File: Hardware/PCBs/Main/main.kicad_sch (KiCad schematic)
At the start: 141 parts, among them J2 HARWIN M20-8890545R, J3 USB4110-GF-A, J4 F3311A7H121010E200, SW1 TL1014BF160QG, SW10 EVPBT1C4A000, SW11 EVPBT1C4A000, SW12 EVPBT1C4A000, SW13 EVPBT1C4A000, SW14 EVPBT1C4A000, SW15 EVPBT1C4A000, SW16 EVPBT1C4A000, SW17 EVPBT1C4A000, SW18 EVPBT1C4A000, SW19 EVPBT1C4A000, SW2 CUS-12TB, SW20 EVPBT1C4A000, SW21 EVPBT1C4A000, SW22 EVPBT1C4A000, SW23 EVPBT1C4A000, SW24 EVPBT1C4A000, SW25 EVPBT1C4A000, SW26 EVPBT1C4A000, SW27 EVPBT1C4A000, SW28 EVPBT1C4A000, SW29 EVPBT1C4A000, SW3 EVPBT1C4A000, SW30 EVPBT1C4A000, SW31 EVPBT1C4A000, SW32 EVPBT1C4A000, SW33 EVPBT1C4A000, SW34 EVPBT1C4A000, SW35 EVPBT1C4A000, SW36 EVPBT1C4A000, SW37 EVPBT1C4A000, SW38 EVPBT1C4A000, SW39 EVPBT1C4A000, SW4 EVPBT1C4A000, SW40 EVPBT1C4A000, SW41 EVPBT1C4A000, SW42 EVPBT1C4A000, SW43 EVPBT1C4A000, SW44 EVPBT1C4A000, SW45 EVPBT1C4A000, SW46 EVPBT1C4A000, SW47 EVPBT1C4A000, SW48 EVPBT1C4A000, SW49 EVPBT1C4A000, SW5 EVPBT1C4A000, SW50 EVPBT1C4A000, SW51 EVPBT1C4A000, SW6 EVPBT1C4A000, SW7 EVPBT1C4A000, SW8 EVPBT1C4A000, SW9 EVPBT1C4A000, U1 STM32U385RGT6Q, U2 TPS61299DRLR, U3 MX25R6435FM2IL0, U4 TLV73333PDBVR, U5 LM66100QDCKRQ1, U6 LM66100QDCKRQ1, U7 NBM5100A, Y1 32768 Hz

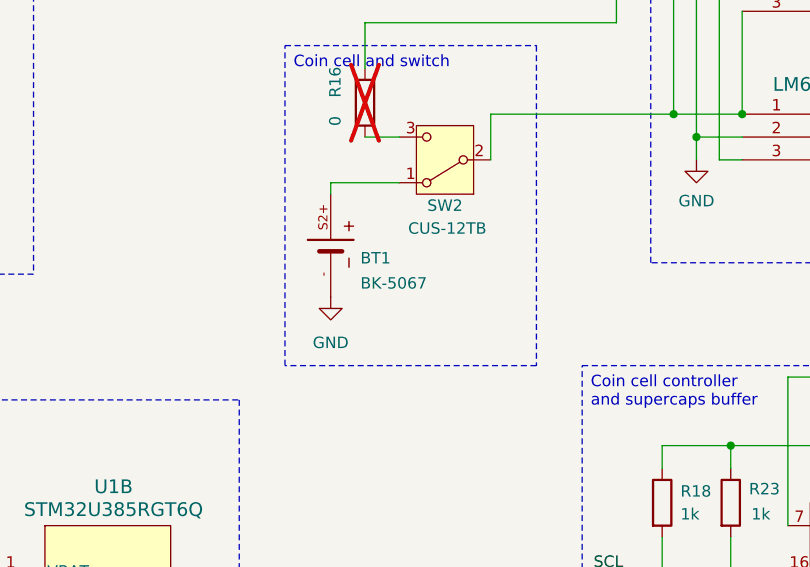
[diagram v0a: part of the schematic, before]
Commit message: Update battery holder part name
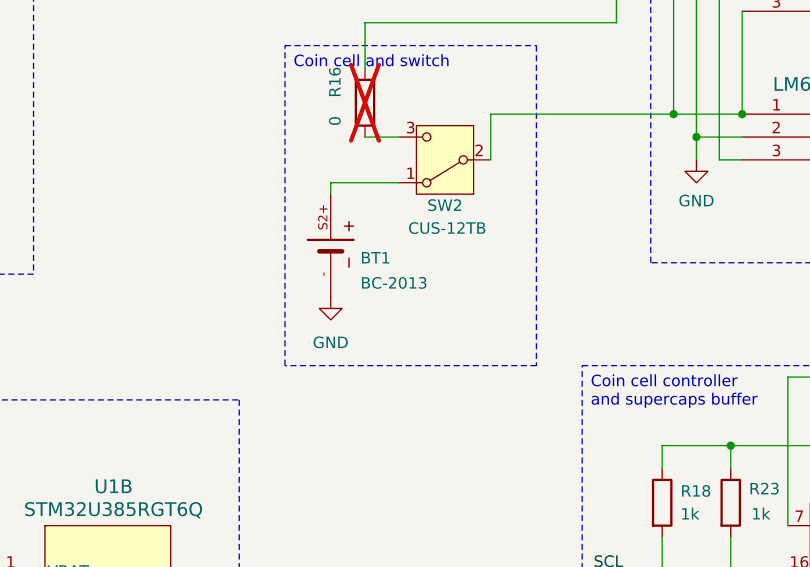
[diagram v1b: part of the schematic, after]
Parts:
- BT1: value BK-5067 -> BC-2013
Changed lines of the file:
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@@
 			)
 		)
-		(property "Value" "BK-5067"
+		(property "Value" "BC-2013"
 			(at 179.832 134.366 90)
 			(effects

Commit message: Bugfix 4.0; added HP48 layout
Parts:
- D1, D2, D3: value NSR0340HT1G -> CDBU0340; footprint Diode_SMD:D_SOD-323_HandSoldering -> Diode_SMD:D_0603_1608Metric_Pad1.05x0.95mm_HandSolder
- U2: footprint Package_TO_SOT_SMD:Texas_R-PDSO-G6 -> Package_TO_SOT_SMD:SOT-563
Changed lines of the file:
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@@
 			)
 		)
-		(property "Value" "NSR0340HT1G"
-			(at 269.24 89.154 0)
+		(property "Value" "CDBU0340"
+			(at 265.684 89.154 0)
 			(effects
 				(font
@@
 			)
 		)
-		(property "Footprint" "Diode_SMD:D_SOD-323_HandSoldering"
+		(property "Footprint" "Diode_SMD:D_0603_1608Metric_Pad1.05x0.95mm_HandSolder"
 			(at 257.81 92.71 0)
 			(effects
@@
 		(fields_autoplaced yes)
 		(property "Reference" "D1"
-			(at 185.42 39.0525 90)
+			(at 185.42 39.0524 90)
 			(effects
 				(font
@@
 			)
 		)
-		(property "Value" "NSR0340HT1G"
-			(at 185.42 41.5925 90)
+		(property "Value" "CDBU0340"
+			(at 185.42 41.5924 90)
 			(effects
 				(font
@@
 			)
 		)
-		(property "Footprint" "Diode_SMD:D_SOD-323_HandSoldering"
+		(property "Footprint" "Diode_SMD:D_0603_1608Metric_Pad1.05x0.95mm_HandSolder"
 			(at 182.88 40.64 0)
 			(effects
@@
 			)
 		)
-		(property "Footprint" "Package_TO_SOT_SMD:Texas_R-PDSO-G6"
+		(property "Footprint" "Package_TO_SOT_SMD:SOT-563"
 			(at 81.28 276.86 0)
 			(effects
@@
 			)
 		)
-		(property "Value" "NSR0340HT1G"
+		(property "Value" "CDBU0340"
 			(at 233.172 27.432 0)
 			(effects
@@
 			)
 		)
-		(property "Footprint" "Diode_SMD:D_SOD-323_HandSoldering"
+		(property "Footprint" "Diode_SMD:D_0603_1608Metric_Pad1.05x0.95mm_HandSolder"
 			(at 233.68 30.48 0)
 			(effects
